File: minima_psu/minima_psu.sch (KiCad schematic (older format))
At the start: 23 parts, among them J1 Screw_Terminal_01x03, J2 Screw_Terminal_01x03, J3 Screw_Terminal_01x03, J4 Screw_Terminal_01x02, J5 Screw_Terminal_01x03, J6 Screw_Terminal_01x03

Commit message: Added mechanical components
Signed-off-by: Nenad Radulovic <nenad.b.radulovic@gmail.com>
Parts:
- removed D2, D3: D, symbol Device:D
- removed J2: Screw_Terminal_01x03, symbol Connector:Screw_Terminal_01x03
- removed R2: R, symbol Device:R
- added D1: GBU2508F, Diode_THT:Diode_Bridge_Vishay_GBU, symbol Diode_Bridge:GBU4A
- added J4: Screw_Terminal_01x03, TerminalBlock_Phoenix:TerminalBlock_Phoenix_MKDS-3-3-5.08_1x03_P5.08mm_Horizontal, symbol Connector:Screw_Terminal_01x03
- added MH1, MH2, MH3, MH4: MountingHole, MountingHole:MountingHole_3.2mm_M3_ISO7380_Pad, symbol Mechanical:MountingHole
- added R5: 10k, Resistor_THT:R_Axial_DIN0207_L6.3mm_D2.5mm_P10.16mm_Horizontal, symbol Device:R
- D2: renamed from D1; value D_Bridge_+-AA -> GBU2508F; footprint (none) -> Diode_THT:Diode_Bridge_Vishay_GBU; symbol Device:D_Bridge_+-AA -> Diode_Bridge:GBU4A; Manufacturer (none) -> Multicomp:GBU2508F; Vendor (none) -> Farnell:2750918
- J1, J3, J5, J6: footprint (none) -> TerminalBlock_Phoenix:TerminalBlock_Phoenix_MKDS-3-3-5.08_1x03_P5.08mm_Horizontal; Manufacturer (none) -> Phoenix:MKDS1/3-3,5; Vendor (none) -> Farnell:2478587
- J2: renamed from J4; footprint (none) -> TerminalBlock_Phoenix:TerminalBlock_Phoenix_MKDS-3-2-5.08_1x02_P5.08mm_Horizontal; Manufacturer (none) -> Phoenix:MKDSN2,5/2-5.08; Vendor (none) -> Farnell:1792766
- R2: renamed from R1; value R -> 1; footprint (none) -> Resistor_THT:R_Axial_DIN0207_L6.3mm_D2.5mm_P10.16mm_Horizontal; Manufacturer (none) -> Vishay:SFR2500001008JA500; Power (none) -> 0.4W; Type (none) -> MF; Vendor (none) -> Farnell:9476539
- R3: value R -> 1; footprint (none) -> Resistor_THT:R_Axial_DIN0207_L6.3mm_D2.5mm_P10.16mm_Horizontal; Manufacturer (none) -> Vishay:SFR2500001008JA500; Power (none) -> 0.4W; Type (none) -> MF; Vendor (none) -> Farnell:9476539
- R4: value R -> 10k; footprint (none) -> Resistor_THT:R_Axial_DIN0207_L6.3mm_D2.5mm_P10.16mm_Horizontal; Manufacturer (none) -> Vishay:SFR2500001002JA500; Power (none) -> 0.4W; Type (none) -> MF; Vendor (none) -> Farnell:9476539
- gave numbers to parts that had none: 1
- renumbered C9 to C1, C1 to C2, C6 to C4, C8 to C5, C5 to C6, C2 to C8, R5 to R1
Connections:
- net labels added: Earth_Protective
- net labels removed: Earth
- wire segments 93 -> 98

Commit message: WIP: Layout of PCB.
Signed-off-by: Nenad Radulovic <nenad.b.radulovic@gmail.com>
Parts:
- added LOGO1: Kicad_Logo, Symbol:KiCad-Logo_5mm_Copper, symbol Graphic:Logo_Open_Hardware_Small
- added LOGO2: Kicad_Logo, Symbol:OSHW-Logo2_7.3x6mm_SilkScreen, symbol Graphic:Logo_Open_Hardware_Small
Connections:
- net GNDPWR: now also R3.2, R5.2; no longer R3.1, R5.1
- net vee: now also R5.1; no longer R5.2
- net acs_p: now reaches C2.1, D2.3 (~~), J1.1 (Pin_1)
- net acs_n: now reaches C3.2, D2.2 (~~), J1.3 (Pin_3)
- net at C3.1: now also R3.1; no longer R3.2
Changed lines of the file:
@@
 U 1 1 5B8A491D
 P 2600 2250
-F 0 "R3" H 2670 2387 50  0000 L CNN
-F 1 "1" H 2670 2296 50  0000 L CNN
+F 0 "R3" H 2530 2113 50  0000 R CNN
+F 1 "1" H 2530 2204 50  0000 R CNN
 F 2 "Resistor_THT:R_Axial_DIN0207_L6.3mm_D2.5mm_P10.16mm_Horizontal" V 2530 2250 50  0001 C CNN
 F 3 "https://export.farnell.com/c/passive-components/resistors-fixed-value/through-hole-resistors?product-range=sfr125-series" H 2600 2250 50  0001 C CNN
 F 4 "Vishay:SFR2500001008JA500" H 2600 2250 50  0001 C CNN "Manufacturer"
 F 5 "Farnell:9476539" H 2600 2250 50  0001 C CNN "Vendor"
-F 6 "0.4W" H 2670 2205 50  0000 L CNN "Power"
-F 7 "MF" H 2670 2114 50  0000 L CNN "Type"
+F 6 "0.4W" H 2530 2295 50  0000 R CNN "Power"
+F 7 "MF" H 2530 2386 50  0000 R CNN "Type"
 	1    2600 2250
-	1    0    0    -1
+	-1   0    0    1
 $EndComp
 $Comp
@@
 U 1 1 5B8A4C40
 P 4600 2750
-F 0 "R5" H 4670 2887 50  0000 L CNN
-F 1 "10k" H 4670 2796 50  0000 L CNN
+F 0 "R5" H 4530 2613 50  0000 R CNN
+F 1 "10k" H 4530 2704 50  0000 R CNN
 F 2 "Resistor_THT:R_Axial_DIN0207_L6.3mm_D2.5mm_P10.16mm_Horizontal" V 4530 2750 50  0001 C CNN
 F 3 "https://export.farnell.com/c/passive-components/resistors-fixed-value/through-hole-resistors?product-range=sfr125-series" H 4600 2750 50  0001 C CNN
 F 4 "Vishay:SFR2500001002JA500" H 4600 2750 50  0001 C CNN "Manufacturer"
 F 5 "Farnell:9476539" H 4600 2750 50  0001 C CNN "Vendor"
-F 6 "0.4W" H 4670 2705 50  0000 L CNN "Power"
-F 7 "MF" H 4670 2614 50  0000 L CNN "Type"
+F 6 "0.4W" H 4530 2795 50  0000 R CNN "Power"
+F 7 "MF" H 4530 2886 50  0000 R CNN "Type"
 	1    4600 2750
-	1    0    0    -1
+	-1   0    0    1
 $EndComp
 $Comp
@@
 $EndComp
 $Comp
-L Graphic:Logo_Open_Hardware_Small #LOGO1
+L Graphic:Logo_Open_Hardware_Small LOGO1
 U 1 1 5B8B640D
 P 10150 4000
-F 0 "#LOGO1" H 10150 4275 50  0001 C CNN
+F 0 "LOGO1" H 10150 4275 50  0001 C CNN
 F 1 "Kicad_Logo" H 10150 4294 50  0000 C CNN
 F 2 "Symbol:KiCad-Logo_5mm_Copper" H 10150 4000 50  0001 C CNN
@@
 $EndComp
 $Comp
-L Graphic:Logo_Open_Hardware_Small #LOGO2
+L Graphic:Logo_Open_Hardware_Small LOGO2
 U 1 1 5B8B650F
 P 10150 4500
-F 0 "#LOGO2" H 10150 4775 50  0001 C CNN
+F 0 "LOGO2" H 10150 4775 50  0001 C CNN
 F 1 "Kicad_Logo" H 10150 4794 50  0000 C CNN
 F 2 "Symbol:OSHW-Logo2_7.3x6mm_SilkScreen" H 10150 4500 50  0001 C CNN
@@
 	1    0    0    -1
 $EndComp
+Text Label 2150 1100 0    50   ~ 0
+acs_p
+Text Label 2150 2900 0    50   ~ 0
+acs_n
+$Comp
+L power:PWR_FLAG #FLG?
+U 1 1 5C4C46CF
+P 2600 1100
+F 0 "#FLG?" H 2600 1175 50  0001 C CNN
+F 1 "PWR_FLAG" H 2600 1274 50  0000 C CNN
+F 2 "" H 2600 1100 50  0001 C CNN
+F 3 "~" H 2600 1100 50  0001 C CNN
+	1    2600 1100
+	1    0    0    -1
+$EndComp
+$Comp
+L power:PWR_FLAG #FLG?
+U 1 1 5C4C470E
+P 2600 2900
+F 0 "#FLG?" H 2600 2975 50  0001 C CNN
+F 1 "PWR_FLAG" H 2600 3074 50  0000 C CNN
+F 2 "" H 2600 2900 50  0001 C CNN
+F 3 "~" H 2600 2900 50  0001 C CNN
+	1    2600 2900
+	-1   0    0    1
+$EndComp
 $EndSCHEMATC

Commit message: WIP: Component routing & placement
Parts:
- removed J6: Screw_Terminal_01x03, TerminalBlock_Phoenix:TerminalBlock_Phoenix_MKDS-3-3-5.08_1x03_P5.08mm_Horizontal, symbol Connector:Screw_Terminal_01x03
- added C3, C4, C7, C8: 100n, Capacitor_THT:C_Rect_L7.0mm_W3.5mm_P5.00mm, symbol Device:C
- added J3: psupply, Connector_Phoenix_MC:PhoenixContact_MCV_1,5_3-G-3.81_1x03_P3.81mm_Vertical, symbol Connector:Screw_Terminal_01x03
- J1: value Screw_Terminal_01x03 -> power; footprint TerminalBlock_Phoenix:TerminalBlock_Phoenix_MKDS-3-3-5.08_1x03_P5.08mm_Horizontal -> Connector_Phoenix_MC:PhoenixContact_MCV_1,5_3-G-3.81_1x03_P3.81mm_Vertical; Manufacturer Phoenix:MKDS1/3-3,5 -> Phoenix: 1803439 (MCV 1,5/ 3-G-3,81); Vendor Farnell:2478587 -> Farnell: 3913089
- J2: renamed from J5; value Screw_Terminal_01x03 -> psupply; footprint TerminalBlock_Phoenix:TerminalBlock_Phoenix_MKDS-3-3-5.08_1x03_P5.08mm_Horizontal -> Connector_Phoenix_MC:PhoenixContact_MCV_1,5_3-G-3.81_1x03_P3.81mm_Vertical; Manufacturer Phoenix:MKDS1/3-3,5 -> Phoenix: 1803439 (MCV 1,5/ 3-G-3,81); Vendor Farnell:2478587 -> Farnell: 3913089
- J4: renamed from J2; value Screw_Terminal_01x02 -> switch
- J5: renamed from J3; value Screw_Terminal_01x03 -> ac_in
- J6: renamed from J4; value Screw_Terminal_01x03 -> transformer
- renumbered C2 to C1, C4 to C10, C7 to C11, C5 to C12, C1 to C13, C8 to C2, C3 to C5, C9 to C6, C6 to C9, D2 to D1, D1 to D2, MH3 to MH2, MH2 to MH3, R2 to R1, R3 to R2, R4 to R3, R5 to R4, R1 to R5
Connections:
- net GNDPWR: now also C3.2, C4.2, C7.1, C8.1, J3.2 (Pin_2)
- net ac_l: now also J4.1 (Pin_1); no longer J4.2 (Pin_2)
- net vcc: now also C3.1, C4.1, J3.1 (Pin_1)
- net vee: now also C7.2, C8.2, J3.3 (Pin_3)
- net at C11.2, C9.1, J6.1 (Pin_1): now also J4.2 (Pin_2); no longer J4.1 (Pin_1)
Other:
- moved on the sheet: J2, J4, R3, R4

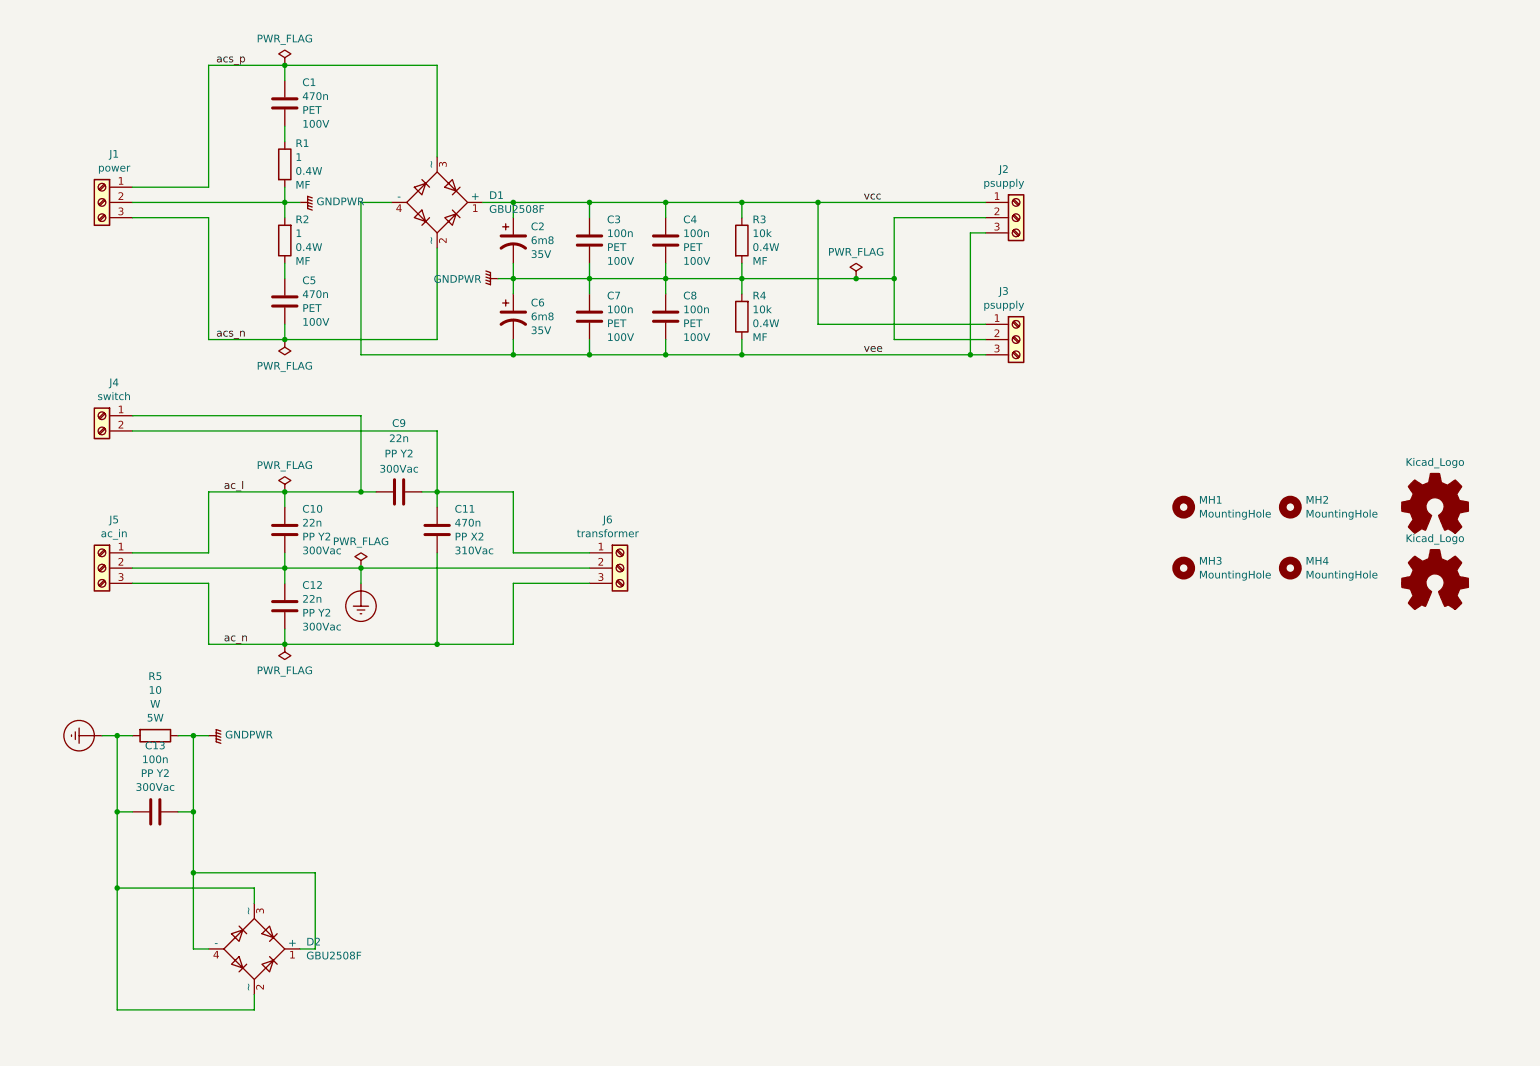
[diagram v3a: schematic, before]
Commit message: Added comment about matching connector
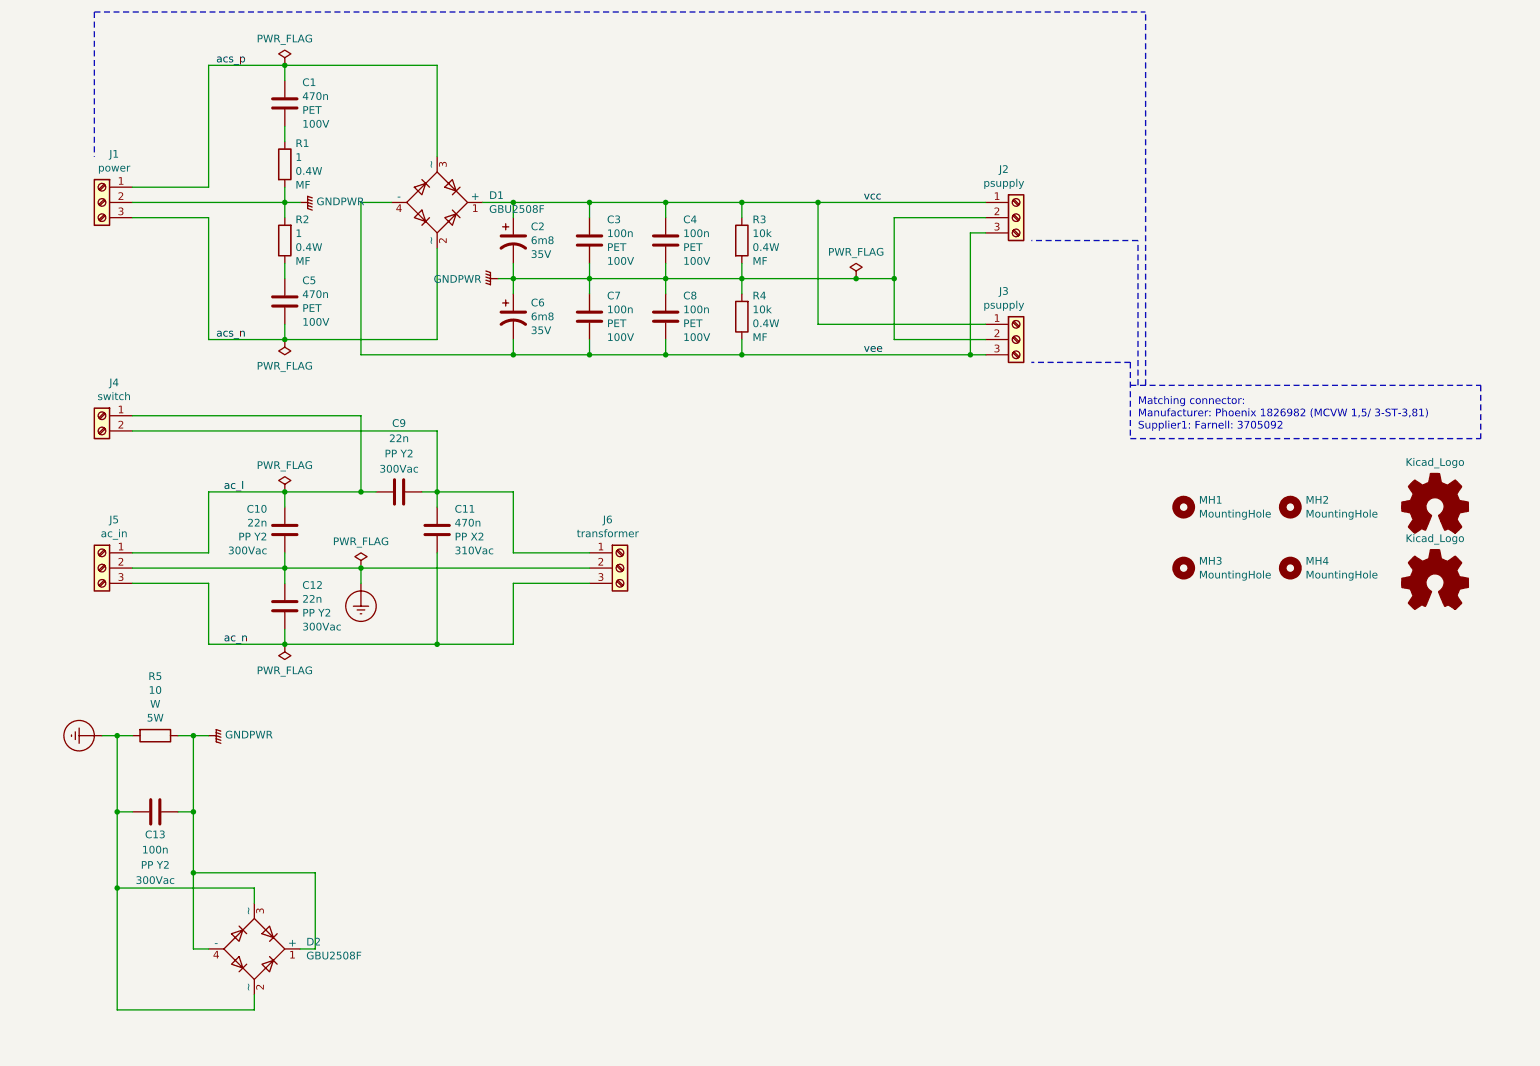
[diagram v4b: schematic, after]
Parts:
- C11: Manufacturer (none) -> Vishay:BFC233922474; Manufacturer: Vishay:BFC233922474 -> (none)
- C13: Manufacturer (none) -> Vishay:BFC233860104; Manufacturer: Vishay:BFC233860104 -> (none)
- R5: Manufacturer (none) -> Vishay:AC05000001009JAC00; Manufacturer: Vishay:AC05000001009JAC00 -> (none)
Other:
- note added: "Matching connector:\nManufacturer: Phoenix 1826982 (MCVW 1,5/ 3-ST-3,81)\nSupplier1: Farnell: 3705092"
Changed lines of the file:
@@
 F 2 "Resistor_THT:R_Axial_DIN0918_L18.0mm_D9.0mm_P22.86mm_Horizontal" V 1680 5500 50  0001 C CNN
 F 3 "http://www.farnell.com/datasheets/2045934.pdf" H 1750 5500 50  0001 C CNN
-F 4 "Vishay:AC05000001009JAC00" V 1750 5500 50  0001 C CNN "Manufacturer:"
+F 4 "Vishay:AC05000001009JAC00" V 1750 5500 50  0001 C CNN "Manufacturer"
 F 5 "Farnel:1735130" V 1750 5500 50  0001 C CNN "Vendor"
 F 6 "W" V 1543 5500 50  0000 C CNN "Type"
@@
 U 1 1 5B6BC17F
 P 1750 6000
-F 0 "C13" V 1316 6000 50  0000 C CNN
-F 1 "100n" V 1407 6000 50  0000 C CNN
+F 0 "C13" V 1900 6000 50  0000 C CNN
+F 1 "100n" V 2000 6000 50  0000 C CNN
 F 2 "Capacitor_THT:C_Rect_L26.5mm_W10.5mm_P22.50mm_MKS4" H 1788 5850 50  0001 C CNN
 F 3 "http://www.farnell.com/datasheets/2237778.pdf" H 1750 6000 50  0001 C CNN
-F 4 "Vishay:BFC233860104" V 1750 6000 50  0001 C CNN "Manufacturer:"
+F 4 "Vishay:BFC233860104" V 1750 6000 50  0001 C CNN "Manufacturer"
 F 5 "Farnell:1166503" V 1750 6000 50  0001 C CNN "Vendor"
-F 6 "PP Y2" V 1498 6000 50  0000 C CNN "Type"
-F 7 "300Vac" V 1589 6000 50  0000 C CNN "Voltage"
+F 6 "PP Y2" V 2100 6000 50  0000 C CNN "Type"
+F 7 "300Vac" V 2200 6000 50  0000 C CNN "Voltage"
 	1    1750 6000
 	0    1    1    0
@@
 U 1 1 5B6C8A78
 P 2600 4150
-F 0 "C10" H 2715 4287 50  0000 L CNN
-F 1 "22n" H 2715 4196 50  0000 L CNN
+F 0 "C10" H 2485 4287 50  0000 R CNN
+F 1 "22n" H 2485 4196 50  0000 R CNN
 F 2 "Capacitor_THT:C_Rect_L18.0mm_W7.0mm_P15.00mm_FKS3_FKP3" H 2638 4000 50  0001 C CNN
 F 3 "http://www.farnell.com/datasheets/2237778.pdf" H 2600 4150 50  0001 C CNN
 F 4 "Vishay:BFC233860223" H 2600 4150 50  0001 C CNN "Manufacturer"
 F 5 "Farnell:1166495" H 2600 4150 50  0001 C CNN "Vendor"
-F 6 "PP Y2" H 2715 4105 50  0000 L CNN "Type"
-F 7 "300Vac" H 2715 4014 50  0000 L CNN "Voltage"
+F 6 "PP Y2" H 2485 4105 50  0000 R CNN "Type"
+F 7 "300Vac" H 2485 4014 50  0000 R CNN "Voltage"
 	1    2600 4150
 	1    0    0    -1
@@
 F 2 "Capacitor_THT:C_Rect_L18.0mm_W11.0mm_P15.00mm_FKS3_FKP3" H 3638 4000 50  0001 C CNN
 F 3 "http://www.farnell.com/datasheets/2047268.pdf" H 3600 4150 50  0001 C CNN
-F 4 "Vishay:BFC233922474" V 3600 4150 50  0001 C CNN "Manufacturer:"
+F 4 "Vishay:BFC233922474" V 3600 4150 50  0001 C CNN "Manufacturer"
 F 5 "Farnell:1413841" V 3600 4150 50  0001 C CNN "Vendor"
 F 6 "PP X2" H 3485 4195 50  0000 R CNN "Type"
@@
 Wire Wire Line
 	5100 2900 5100 3000
+Text Notes 8200 3500 0    50   ~ 0
+Matching connector:\nManufacturer: Phoenix 1826982 (MCVW 1,5/ 3-ST-3,81)\nSupplier1: Farnell: 3705092
+Wire Notes Line
+	8150 3200 10450 3200
+Wire Notes Line
+	10450 3200 10450 3550
+Wire Notes Line
+	8150 3550 10450 3550
+Wire Notes Line
+	1350 750  1350 1700
+Wire Notes Line
+	8150 3050 7500 3050
+Wire Notes Line
+	8150 3050 8150 3550
+Wire Notes Line
+	8200 3200 8200 2250
+Wire Notes Line
+	8200 2250 7500 2250
+Wire Notes Line
+	8250 3200 8250 750
+Wire Notes Line
+	1350 750  8250 750
 $EndSCHEMATC
